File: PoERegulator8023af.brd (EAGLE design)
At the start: 30.5 x 33 mm, 9 parts, among them J1 SJCN

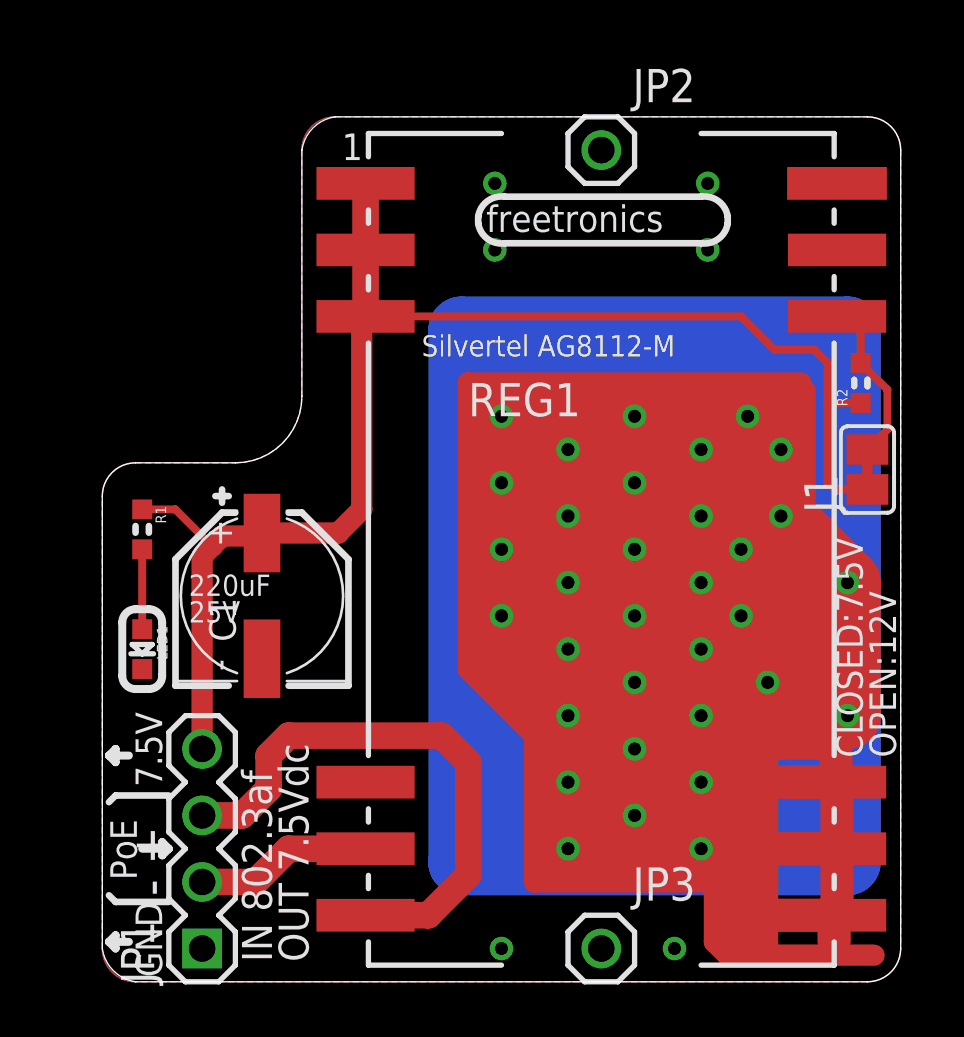
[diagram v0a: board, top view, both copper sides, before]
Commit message: Replaced Silvertel AG8112M with AG9812M for v2.0 release
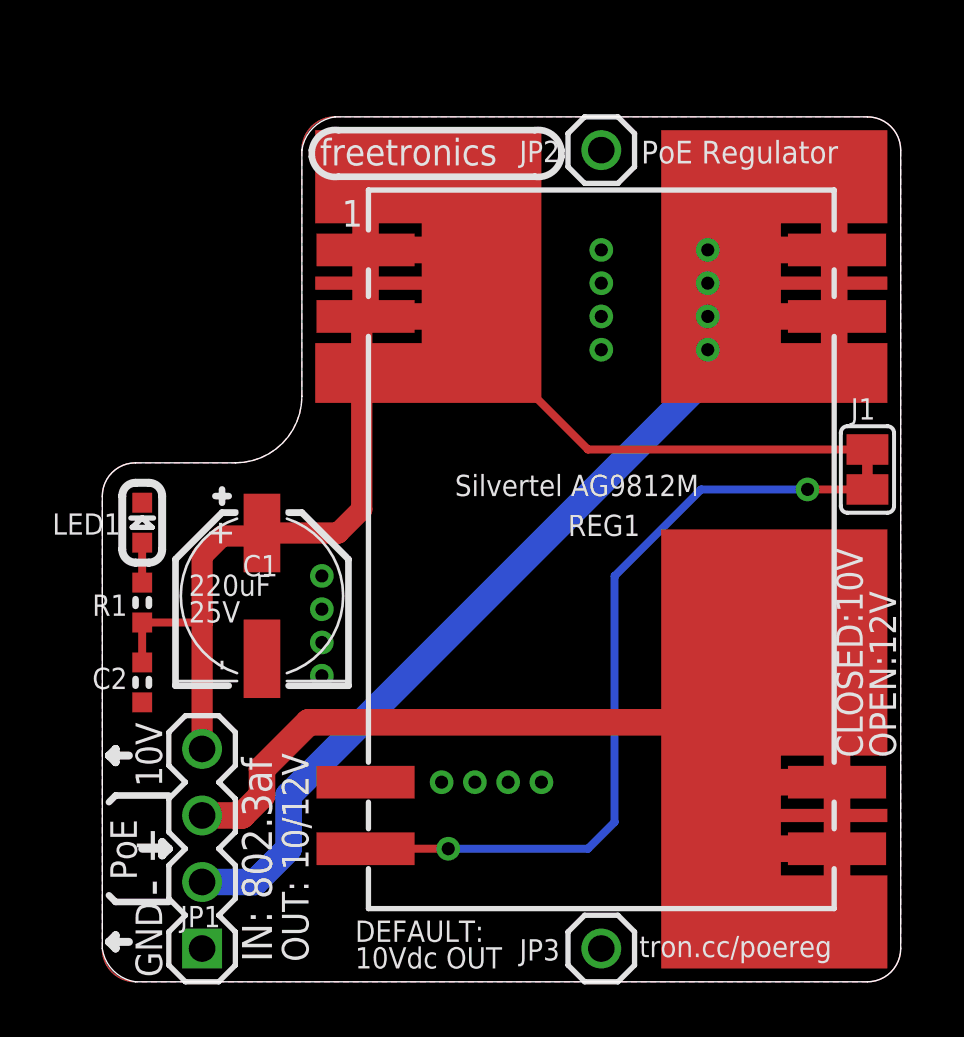
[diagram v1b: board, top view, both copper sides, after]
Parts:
- removed R2: 68K 1%, freetronics:0603
- added C2: 100nF 0603, freetronics-master-v1.1:0603
- R1: value 1K5 -> 2K2
- REG1: value AG8100SMT -> AG9800; device freetronics-master-v1:AG8100 -> freetronics-jon:AG9800
- moved LED1 4.83 mm to (1.52, 17.5), turned to 90 degrees
- moved R1 2.79 mm to (1.52, 14.5), turned to 90 degrees
- turned J1 to 270 degrees
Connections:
- removed net N$2: J1.2, R2.2, REG1.P10
- removed net N$5: JP1.2, REG1.P5
- removed net TGND: REG1.P7, REG1.P8, REG1.P9
- removed net VIN: C1.+, J1.1, JP1.4, R1.1, R2.1, REG1.P1, REG1.P2, REG1.P3
- new net +VDC: C1.+, C2.1, J1.1, JP1.4, R1.1, REG1.P1, REG1.P2
- new net VIN+: JP1.3, REG1.P5, REG1.P6
- new net VIN-: JP1.2, REG1.P7, REG1.P8
- net GND: now also C2.2, REG1.P3; no longer REG1.P11, REG1.P12
- net N$1: now also J1.2, REG1.P4; no longer JP1.3, REG1.P6
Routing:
- net TGND: track 499.7 -> 0.00 mm, vias 33 -> 0
- net +VDC: track 0.00 -> 58.6 mm
- net VIN: track 55.7 -> 0.00 mm
- net VIN-: track 0.00 -> 54.2 mm, vias 0 -> 4
- net VIN+: track 0.00 -> 39.7 mm
- net N$1: track 21.5 -> 30.3 mm, vias 0 -> 2
- net N$5: track 6.77 -> 0.00 mm
- net N$2: track 6.72 -> 0.00 mm
- net N$131: track 3.05 -> 1.52 mm
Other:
- board text added: "(c) 2013 Freetronics Pty Ltd"
- board text added: "10V"
- board text added: "10Vdc OUT"
- board text added: "A"
- board text added: "CLOSED:10V"
- board text added: "DEFAULT:"
- board text added: "IN: 802.3af"
- board text added: "K"
- board text added: "OUT: 10/12V"
- board text added: "PoE Regulator"
- board text added: "SKU: POEREG v2.0"
- board text added: "Silvertel AG9812M"
- board text added: "tron.cc/poereg"
- board text removed: "(c) 2010 Freetronics"
- board text removed: "7.5V"
- board text removed: "CLOSED:7.5V"
- board text removed: "IN 802.3af"
- board text removed: "OUT 7.5Vdc"
- board text removed: "POE-REG-8023AF v2.0"
- board text removed: "Silvertel AG8112-M"
- board text removed: "www.freetronics.com/poe-regulator-8023af"
